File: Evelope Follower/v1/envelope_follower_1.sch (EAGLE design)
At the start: 8 parts, among them J1 MJ-3536N, J2 MJ-3536N, J3 OSTVN03A150

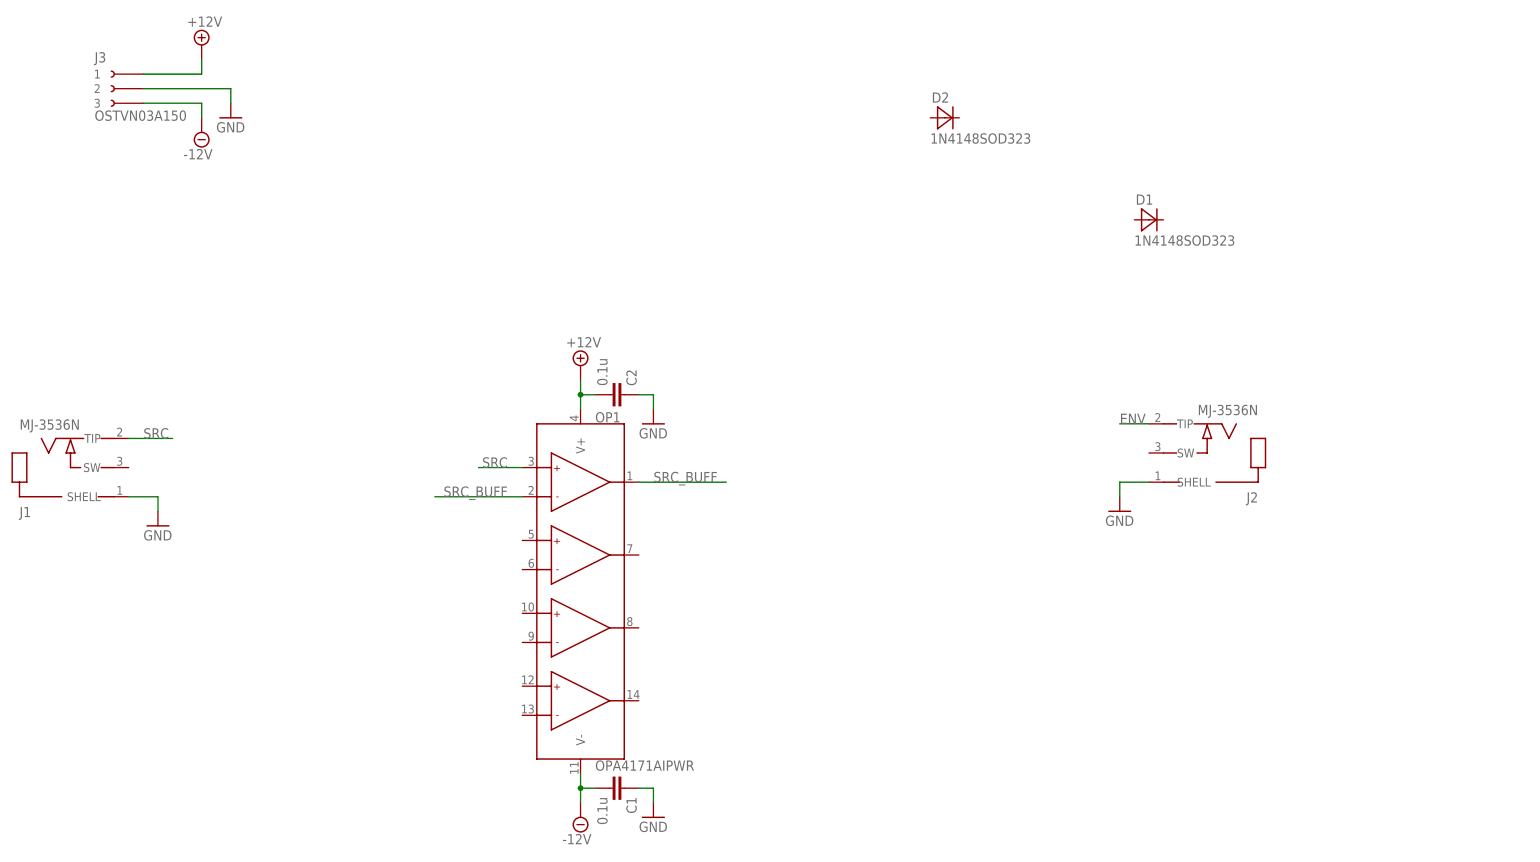
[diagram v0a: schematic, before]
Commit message: Basic circuit/layout captured
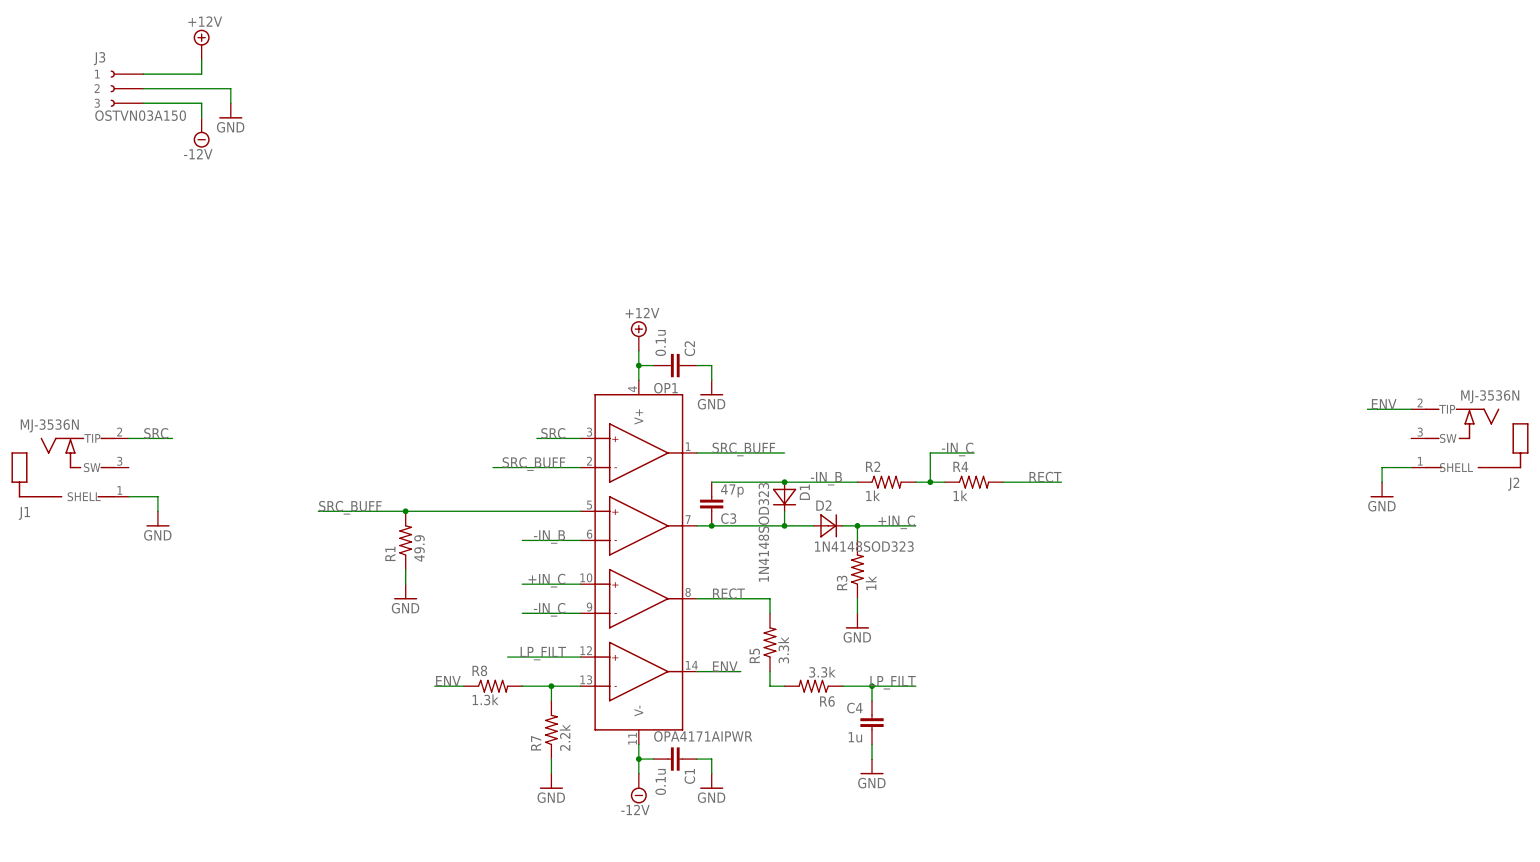
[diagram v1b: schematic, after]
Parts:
- added C3: 47p, roomready:CAP-CER-SMD0603
- added C4: 1u, roomready:CAP-CER-SMD0603
- added R1: 49.9, roomready:RES-SMD0603
- added R2, R3, R4: 1k, roomready:RES-SMD0603
- added R5, R6: 3.3k, roomready:RES-SMD0603
- added R7: 2.2k, roomready:RES-SMD0603
- added R8: 1.3k, roomready:RES-SMD0603
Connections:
- new net +IN_C: D2.C, OP1.+IN_C, R3.2
- new net -IN_B: C3.2, D1.A, OP1.-IN_B, R2.1
- new net -IN_C: OP1.-IN_C, R2.2, R4.1
- new net LP_FILT: C4.1, OP1.+IN_D, R6.1
- new net N$1: C3.1, D1.C, D2.A, OP1.OUT_B
- new net N$2: R5.1, R6.2
- new net N$3: OP1.-IN_D, R7.2, R8.2
- new net RECT: OP1.OUT_C, R4.2, R5.2
- net ENV: now also OP1.OUT_D, R8.1
- net GND: now also C4.2, R1.1, R3.1, R7.1
- net SRC_BUFF: now also OP1.+IN_B, R1.2
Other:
- moved on the sheet: C1, C2, D1, D2, J2, OP1

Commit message: more changes
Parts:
- added TP1, TP2, TP3, TP4, TP5, TP6, TP7, TP8: (no value), roomready:TP_THM_1.6_S
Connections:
- net ENV: now also TP3.TP
- net GND: now also TP2.TP, TP4.TP, TP8.TP
- net LP_FILT: now also TP7.TP
- net RECT: now also TP6.TP
- net SRC: now also TP1.TP
- net SRC_BUFF: now also TP5.TP
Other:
- note added: "MAKE A POT"
- moved on the sheet: J3, R1

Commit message: ch-ch-ch-c
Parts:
- added J4: OSTVN02A150, roomready:OSTVN02A150
- R6: value 3.3k -> DNP
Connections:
- net LP_FILT: now also R5.2; no longer R6.1
- net N$2: now also J4.2
- net RECT: now also J4.1, R6.1; no longer R5.2
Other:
- note added: "3.3k Pot"
- note removed: "MAKE A POT"
- moved on the sheet: R5, R6
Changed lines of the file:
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@@
 <part name="R4" library="roomready" library_urn="urn:adsk.eagle:library:9911636" deviceset="RES-SMD" device="0603" package3d_urn="urn:adsk.eagle:package:7587835/3" value="1k"/>
 <part name="R5" library="roomready" library_urn="urn:adsk.eagle:library:9911636" deviceset="RES-SMD" device="0603" package3d_urn="urn:adsk.eagle:package:7587835/3" value="3.3k"/>
-<part name="R6" library="roomready" library_urn="urn:adsk.eagle:library:9911636" deviceset="RES-SMD" device="0603" package3d_urn="urn:adsk.eagle:package:7587835/3" value="3.3k"/>
 <part name="C4" library="roomready" library_urn="urn:adsk.eagle:library:9911636" deviceset="CAP-CER-SMD" device="0603" package3d_urn="urn:adsk.eagle:package:7587834/2" value="1u"/>
 <part name="GND8" library="supply1" library_urn="urn:adsk.eagle:library:371" deviceset="GND" device=""/>
@@
 <part name="TP8" library="roomready" library_urn="urn:adsk.eagle:library:9911636" deviceset="TP_THM_1.6_S" device="" package3d_urn="urn:adsk.eagle:package:10068194/3"/>
 <part name="GND10" library="supply1" library_urn="urn:adsk.eagle:library:371" deviceset="GND" device=""/>
+<part name="J4" library="roomready" library_urn="urn:adsk.eagle:library:9911636" deviceset="OSTVN02A150" device="" package3d_urn="urn:adsk.eagle:package:12594929/2"/>
+<part name="R6" library="roomready" library_urn="urn:adsk.eagle:library:9911636" deviceset="RES-SMD" device="0603" package3d_urn="urn:adsk.eagle:package:7587835/3" value="DNP"/>
 </parts>
 <sheets>
 <sheet>
 <plain>
-<text x="88.9" y="2.54" size="1.778" layer="91">MAKE A POT</text>
+<text x="68.58" y="-5.08" size="1.778" layer="97">3.3k Pot</text>
 </plain>
 <instances>
@@
 <attribute name="NAME" x="115.57" y="37.338" size="1.778" layer="96"/>
 </instance>
-<instance part="R5" gate="G$1" x="83.82" y="7.62" smashed="yes" rot="R90">
-<attribute name="VALUE" x="87.122" y="3.81" size="1.778" layer="96" rot="R90"/>
-<attribute name="NAME" x="82.042" y="3.81" size="1.778" layer="96" rot="R90"/>
-</instance>
-<instance part="R6" gate="G$1" x="91.44" y="0" smashed="yes" rot="R180">
-<attribute name="VALUE" x="95.25" y="3.302" size="1.778" layer="96" rot="R180"/>
-<attribute name="NAME" x="95.25" y="-1.778" size="1.778" layer="96" rot="R180"/>
+<instance part="R5" gate="G$1" x="93.98" y="0" smashed="yes">
+<attribute name="VALUE" x="90.17" y="-3.302" size="1.778" layer="96"/>
+<attribute name="NAME" x="90.17" y="1.778" size="1.778" layer="96"/>
 </instance>
 <instance part="C4" gate="G$1" x="101.6" y="-5.08" smashed="yes" rot="MR0">
@@
 <instance part="GND10" gate="1" x="86.36" y="-20.32" smashed="yes">
 <attribute name="VALUE" x="83.82" y="-22.86" size="1.778" layer="96"/>
+</instance>
+<instance part="J4" gate="G$1" x="81.28" y="-2.54" smashed="yes">
+<attribute name="NAME" x="77.851" y="-0.508" size="1.778" layer="95"/>
+<attribute name="VALUE" x="77.851" y="-8.128" size="1.778" layer="95"/>
+</instance>
+<instance part="R6" gate="G$1" x="88.9" y="7.62" smashed="yes" rot="R270">
+<attribute name="VALUE" x="85.598" y="11.43" size="1.778" layer="96" rot="R270"/>
+<attribute name="NAME" x="90.678" y="11.43" size="1.778" layer="96" rot="R270"/>
 </instance>
 </instances>
@@
 <segment>
 <pinref part="OP1" gate="G$1" pin="OUT_C"/>
-<wire x1="71.12" y1="15.24" x2="83.82" y2="15.24" width="0.1524" layer="91"/>
+<wire x1="71.12" y1="15.24" x2="86.36" y2="15.24" width="0.1524" layer="91"/>
 <label x="73.66" y="15.24" size="1.778" layer="95"/>
-<pinref part="R5" gate="G$1" pin="2"/>
-<wire x1="83.82" y1="15.24" x2="83.82" y2="12.7" width="0.1524" layer="91"/>
-<wire x1="83.82" y1="15.24" x2="86.36" y2="15.24" width="0.1524" layer="91"/>
-<junction x="83.82" y="15.24"/>
 <pinref part="TP6" gate="G$1" pin="TP"/>
 <wire x1="86.36" y1="15.24" x2="86.36" y2="17.78" width="0.1524" layer="91"/>
-</segment>
-</net>
-<net name="N$2" class="0">
-<segment>
-<pinref part="R5" gate="G$1" pin="1"/>
-<wire x1="83.82" y1="2.54" x2="83.82" y2="0" width="0.1524" layer="91"/>
-<wire x1="83.82" y1="0" x2="86.36" y2="0" width="0.1524" layer="91"/>
-<pinref part="R6" gate="G$1" pin="2"/>
+<pinref part="R6" gate="G$1" pin="1"/>
+<wire x1="88.9" y1="12.7" x2="88.9" y2="15.24" width="0.1524" layer="91"/>
+<wire x1="88.9" y1="15.24" x2="86.36" y2="15.24" width="0.1524" layer="91"/>
+<junction x="86.36" y="15.24"/>
+<pinref part="J4" gate="G$1" pin="1"/>
+<wire x1="86.36" y1="-2.54" x2="86.36" y2="15.24" width="0.1524" layer="91"/>
 </segment>
 </net>
@@
 <pinref part="C4" gate="G$1" pin="1"/>
 <wire x1="101.6" y1="-2.54" x2="101.6" y2="0" width="0.1524" layer="91"/>
-<pinref part="R6" gate="G$1" pin="1"/>
-<wire x1="101.6" y1="0" x2="96.52" y2="0" width="0.1524" layer="91"/>
 <wire x1="101.6" y1="0" x2="111.76" y2="0" width="0.1524" layer="91"/>
-<junction x="101.6" y="0"/>
 <label x="109.22" y="0" size="1.778" layer="95" rot="MR0"/>
 <pinref part="TP7" gate="G$1" pin="TP"/>
 <wire x1="111.76" y1="0" x2="111.76" y2="2.54" width="0.1524" layer="91"/>
+<pinref part="R5" gate="G$1" pin="2"/>
+<wire x1="99.06" y1="0" x2="101.6" y2="0" width="0.1524" layer="91"/>
+<junction x="101.6" y="0"/>
 </segment>
 <segment>
@@
 <segment>
 <pinref part="OP1" gate="G$1" pin="OUT_D"/>
-<wire x1="71.12" y1="2.54" x2="78.74" y2="2.54" width="0.1524" layer="91"/>
 <label x="73.66" y="2.54" size="1.778" layer="95"/>
+<wire x1="78.74" y1="2.54" x2="71.12" y2="2.54" width="0.1524" layer="91"/>
 </segment>
 <segment>
@@
 </segment>
 </net>
+<net name="N$2" class="0">
+<segment>
+<pinref part="J4" gate="G$1" pin="2"/>
+<wire x1="86.36" y1="-5.08" x2="88.9" y2="-5.08" width="0.1524" layer="91"/>
+<pinref part="R5" gate="G$1" pin="1"/>
+<wire x1="88.9" y1="-5.08" x2="88.9" y2="0" width="0.1524" layer="91"/>
+<pinref part="R6" gate="G$1" pin="2"/>
+<wire x1="88.9" y1="2.54" x2="88.9" y2="0" width="0.1524" layer="91"/>
+<junction x="88.9" y="0"/>
+</segment>
+</net>
